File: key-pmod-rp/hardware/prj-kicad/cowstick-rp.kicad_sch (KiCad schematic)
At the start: 3 parts, among them J2 PMOD, P1 CONN_USB-A, U1 RP2040

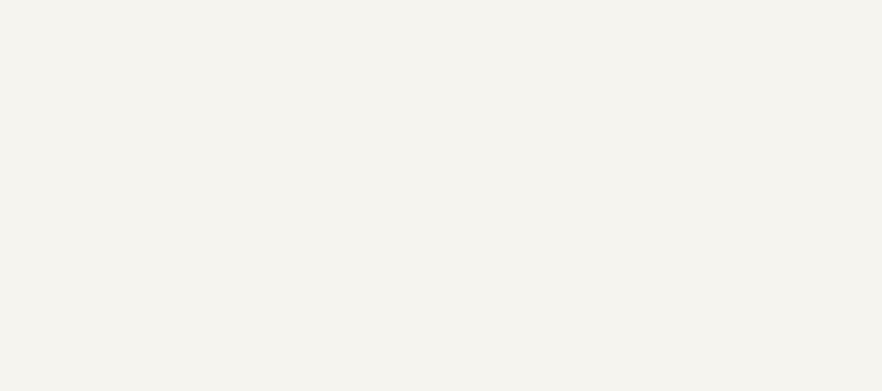
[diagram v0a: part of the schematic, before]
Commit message: KeyPMOD: Improve PCB r1, add power supply (5V->3V3)
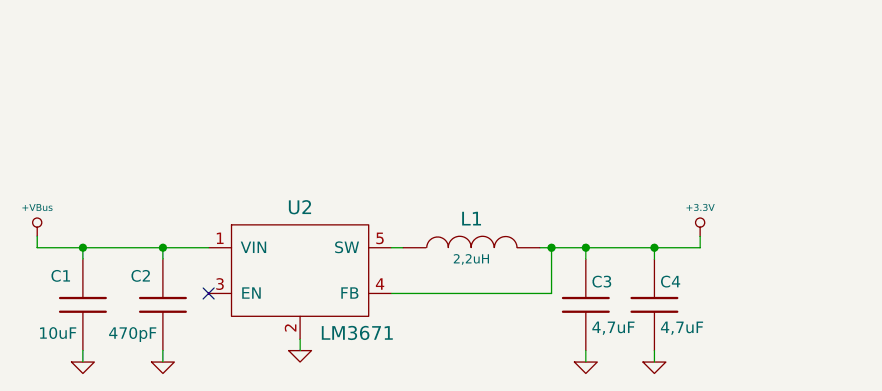
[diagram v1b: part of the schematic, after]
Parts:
- added C1: 10uF, cowstick-rp:SMD0805, symbol cowstick-rp:C
- added C2: 470pF, cowstick-rp:SMD0603, symbol cowstick-rp:C
- added C3, C4: 4,7uF, cowstick-rp:SMD0805, symbol cowstick-rp:C
- added L1: 2,2uH, cowstick-rp:I_CDRH2D14, symbol cowstick-rp:INDUCTOR
- added U2: LM3671, cowstick-rp:SOT23-5, symbol cowstick-rp:LM3671
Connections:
- net +3.3V: now also C3.1, C4.1, L1.2, U2.4 (FB)
- net +VBus: now also C1.1, C2.1, U2.1 (VIN)
- net GND: now also C1.2, C2.2, C3.2, C4.2, U2.2
- new net: L1.1, U2.5 (SW)
- no-connect marks 0 -> 1

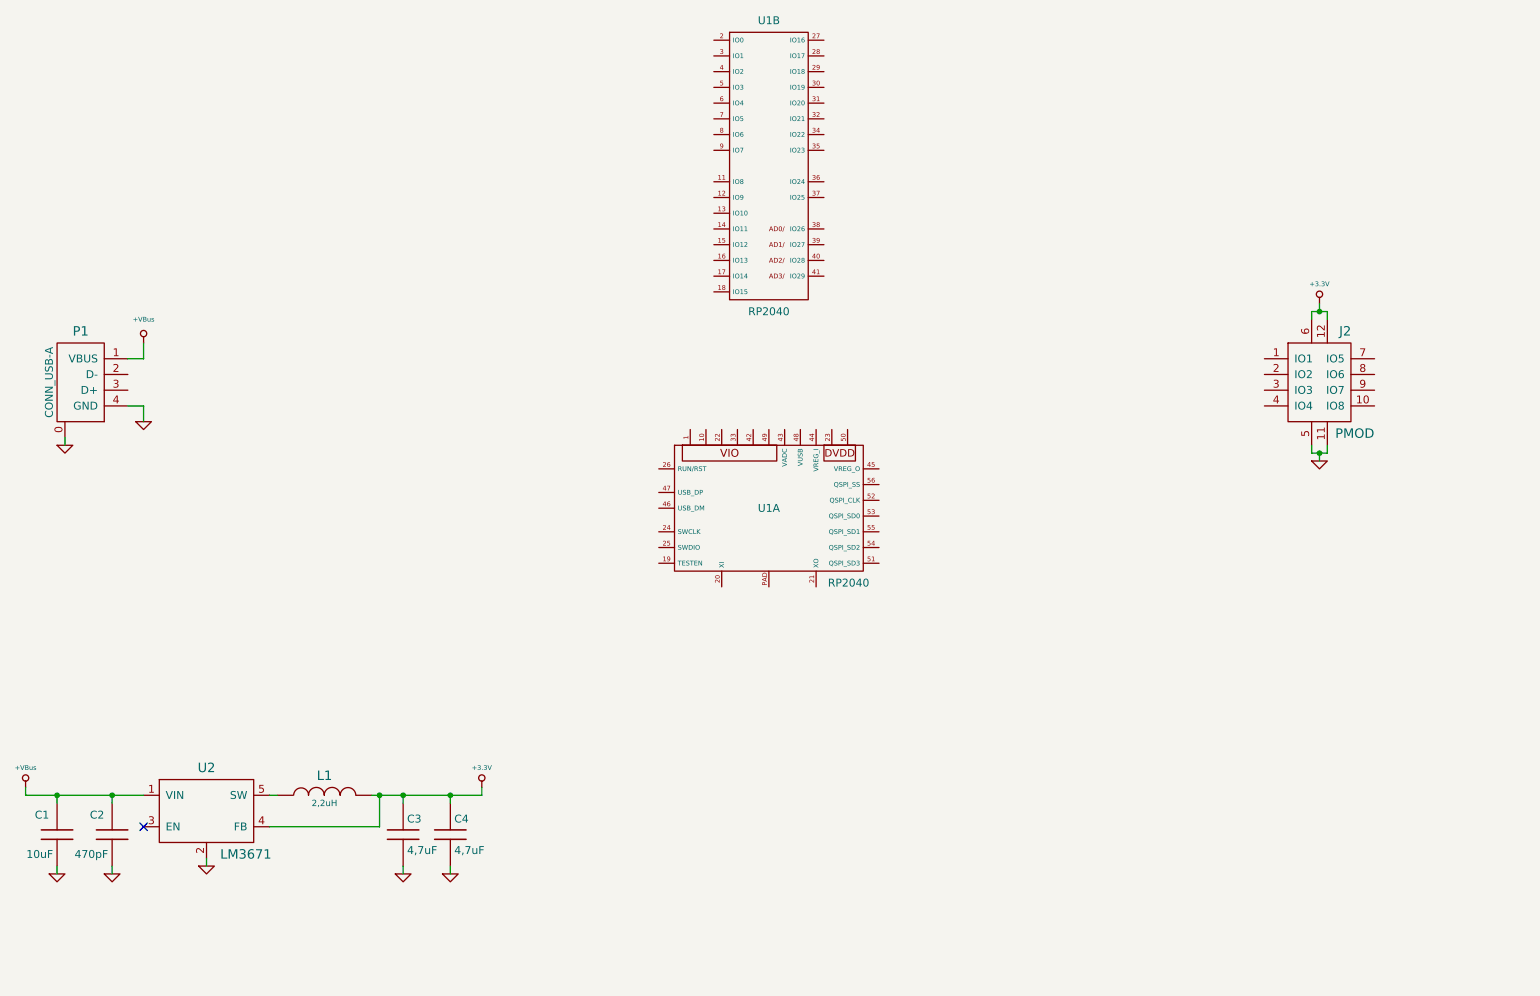
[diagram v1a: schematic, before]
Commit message: KeyPMOD: Improve PCB r1, add RP2040 mcu (include crystal and decoupling caps)
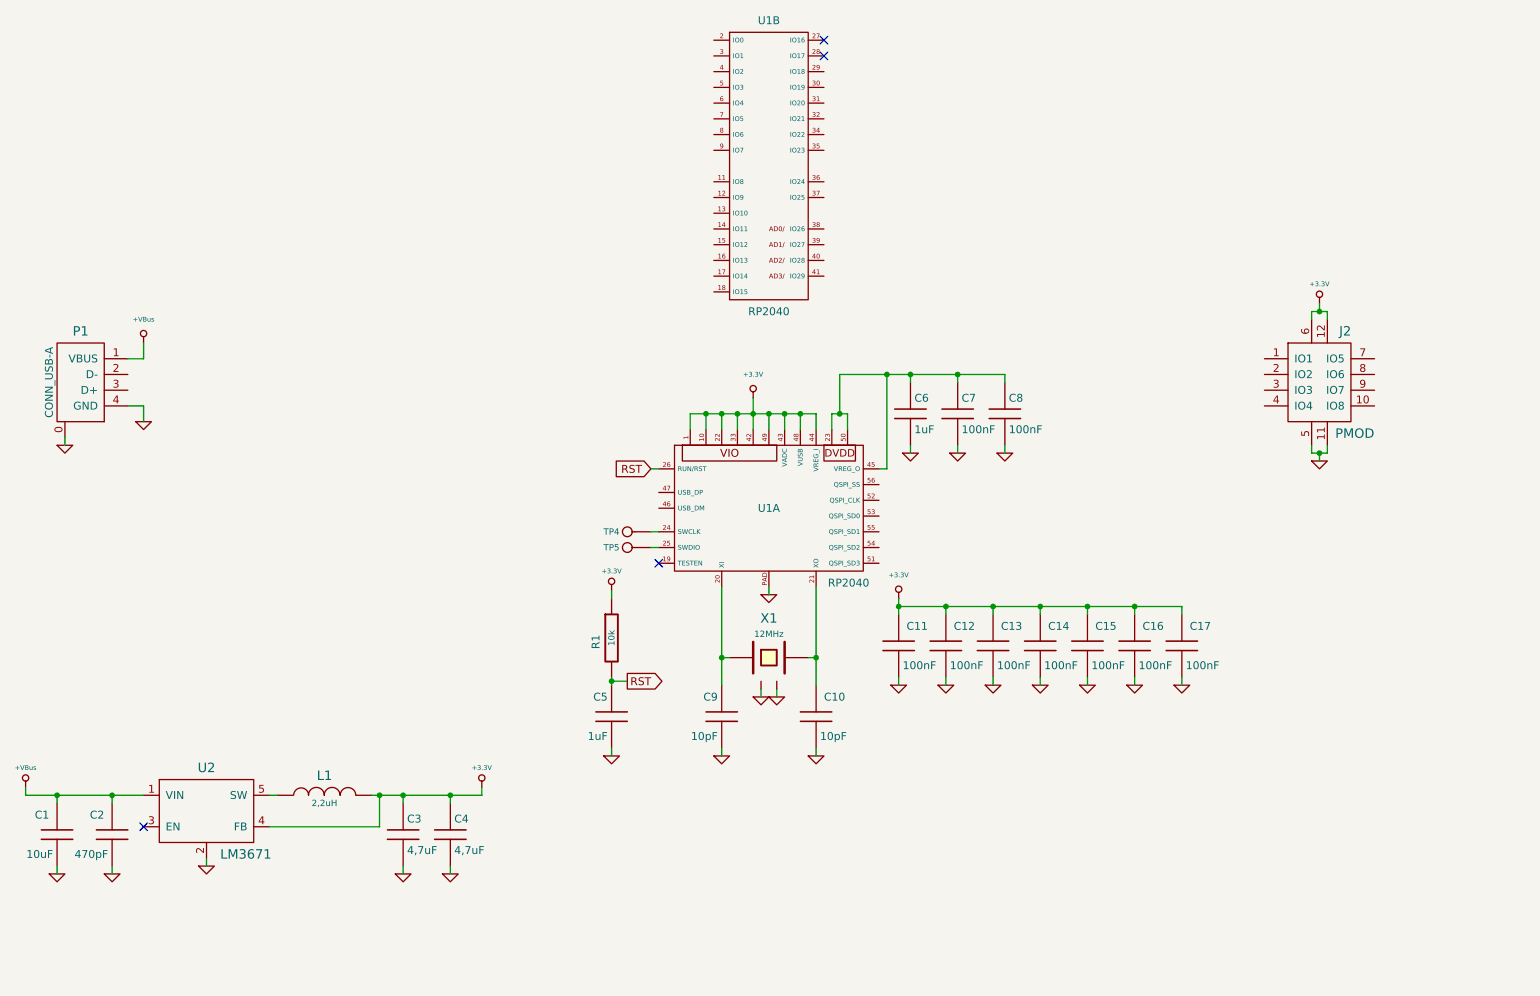
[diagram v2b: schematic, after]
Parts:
- added C10, C9: 10pF, cowstick-rp:SMD0603, symbol cowstick-rp:C
- added C11, C12, C13, C14, C15, C16, C17, C7, C8: 100nF, cowstick-rp:SMD0603, symbol cowstick-rp:C
- added C5, C6: 1uF, cowstick-rp:SMD0603, symbol cowstick-rp:C
- added R1: 10k, cowstick-rp:SMD0603, symbol cowstick-rp:R
- added TP4, TP5: CONN_1, cowstick-rp:TP_SMD, symbol cowstick-rp:CONN_1
- added X1: 12MHz, cowstick-rp:Q_3.2x2.5, symbol cowstick-rp:CRYSTAL4
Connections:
- net +3.3V: now also U1.1, U1.10, U1.22, U1.33, U1.42, U1.43 (VADC), U1.44 (VREG_I), U1.48 (VUSB), U1.49, C11.1, C12.1, C13.1, C14.1, C15.1, C16.1, C17.1, R1.1
- net GND: now also U1.PAD, C10.2, C11.2, C12.2, C13.2, C14.2, C15.2, C16.2, C17.2, C5.2, C6.2, C7.2, C8.2, C9.2, X1.2, X1.4
- net at U1.20 (XI): now also C9.1, X1.1
- net at U1.21 (XO): now also C10.1, X1.3
- net at U1.23: now also U1.45 (VREG_O), U1.50, C6.1, C7.1, C8.1
- net at U1.24 (SWCLK): now also TP4.1
- net at U1.25 (SWDIO): now also TP5.1
- net RST: now reaches U1.26 (RUN/RST)
- net RST: now also C5.1, R1.2
- no-connect marks 1 -> 4

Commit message: KeyPMOD: Add flash memory and USB protection. Design of board rev1 mostly finish
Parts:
- added C18, C19: 100nF, cowstick-rp:SMD0603, symbol cowstick-rp:C
- added C20: 10uF, cowstick-rp:SMD0805, symbol cowstick-rp:C
- added D1: USBLC6-2, cowstick-rp:SOT23-6, symbol cowstick-rp:USBLC6-2
- added D2: LED, cowstick-rp:SMD0805, symbol cowstick-rp:LED
- added JP1: JUMPER, cowstick-rp:TP_JP, symbol cowstick-rp:JUMPER
- added L2: FB100, cowstick-rp:SMD0603, symbol cowstick-rp:INDUCTOR
- added R2, R3: 23, cowstick-rp:SMD0603, symbol cowstick-rp:R
- added R4, R5: 10k, cowstick-rp:SMD0603, symbol cowstick-rp:R
- added R6: 470, cowstick-rp:SMD0603, symbol cowstick-rp:R
- added R7: 1k, cowstick-rp:SMD0603, symbol cowstick-rp:R
- added SW1: SW_PUSH, cowstick-rp:SW_436351045816, symbol cowstick-rp:SW_PUSH
- added TP1, TP3: CONN_1, cowstick-rp:TP_SMD, symbol cowstick-rp:CONN_1
- added U3: W25Q16JV, cowstick-rp:SOIC-8, symbol cowstick-rp:W25Q16JV
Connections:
- net +3.3V: now also C18.1, L2.1, R4.1, R5.1, U3.8; no longer J2.12, J2.6
- net +VBus: now also D1.5
- net GND: now also C18.2, C19.2, C20.2, D1.2, D2.2 (K), SW1.1, TP1.1, U3.4
- net RST: now also TP3.1
- net PMOD_CTS: now reaches J2.1 (IO1)
- net PMOD_CTS: now also U1.13 (IO10)
- net PMOD_IO8: now reaches J2.10 (IO8)
- net PMOD_IO8: now also U1.38 (IO26)
- net PMOD_TX: now reaches J2.2 (IO2)
- net PMOD_TX: now also U1.11 (IO8)
- net PMOD_RX: now reaches J2.3 (IO3)
- net PMOD_RX: now also U1.12 (IO9)
- net PMOD_RTS: now reaches J2.4 (IO4)
- net PMOD_RTS: now also U1.14 (IO11)
- net PMOD_IO5: now reaches J2.7 (IO5)
- net PMOD_IO5: now also U1.41 (IO29)
- net PMOD_IO6: now reaches J2.8 (IO6)
- net PMOD_IO6: now also U1.40 (IO28)
- net PMOD_IO7: now reaches J2.9 (IO7)
- net PMOD_IO7: now also U1.39 (IO27)
- net at P1.2 (D-): now also D1.4 (IO2)
- net at P1.3 (D+): now also D1.6 (IO1)
- net USB_D-: now reaches U1.46 (USB_DM)
- net USB_D-: now also R2.2
- net USB_D+: now reaches U1.47 (USB_DP)
- net USB_D+: now also R3.2
- net FL_D3: now reaches U1.51 (QSPI_SD3)
- net FL_D3: now also U3.7 (IO3_HOLD)
- net FL_SCK: now reaches U1.52 (QSPI_CLK)
- net FL_SCK: now also U3.6 (CLK)
- net FL_D0: now reaches U1.53 (QSPI_SD0)
- net FL_D0: now also U3.5 (IO0_DI)
- net FL_D2: now reaches U1.54 (QSPI_SD2)
- net FL_D2: now also U3.3 (IO2_WP)
- net FL_D1: now reaches U1.55 (QSPI_SD1)
- net FL_D1: now also U3.2 (IO1_DO)
- net UB: now reaches U1.56 (QSPI_SS)
- net UB: now also R4.2, R7.2, U3.1 (CS)
- net BUTTON: now reaches U1.18 (IO15)
- net BUTTON: now also C19.1, JP1.1, R5.2, SW1.2
- net LED: now reaches U1.29 (IO18)
- net LED: now also R6.1
- new net: D1.1 (IO1), R3.1
- new net: D1.3 (IO2), R2.1
- new net: D2.1 (A), R6.2
- new net: JP1.2, R7.1
- new net +PMOD: C20.1, J2.12, J2.6, L2.2
- no-connect marks 4 -> 22
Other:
- moved on the sheet: C1, C11, C12, C13, C14, C15, C16, C17, C2, C3, C4, J2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
